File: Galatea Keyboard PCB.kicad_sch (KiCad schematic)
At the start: 0 parts

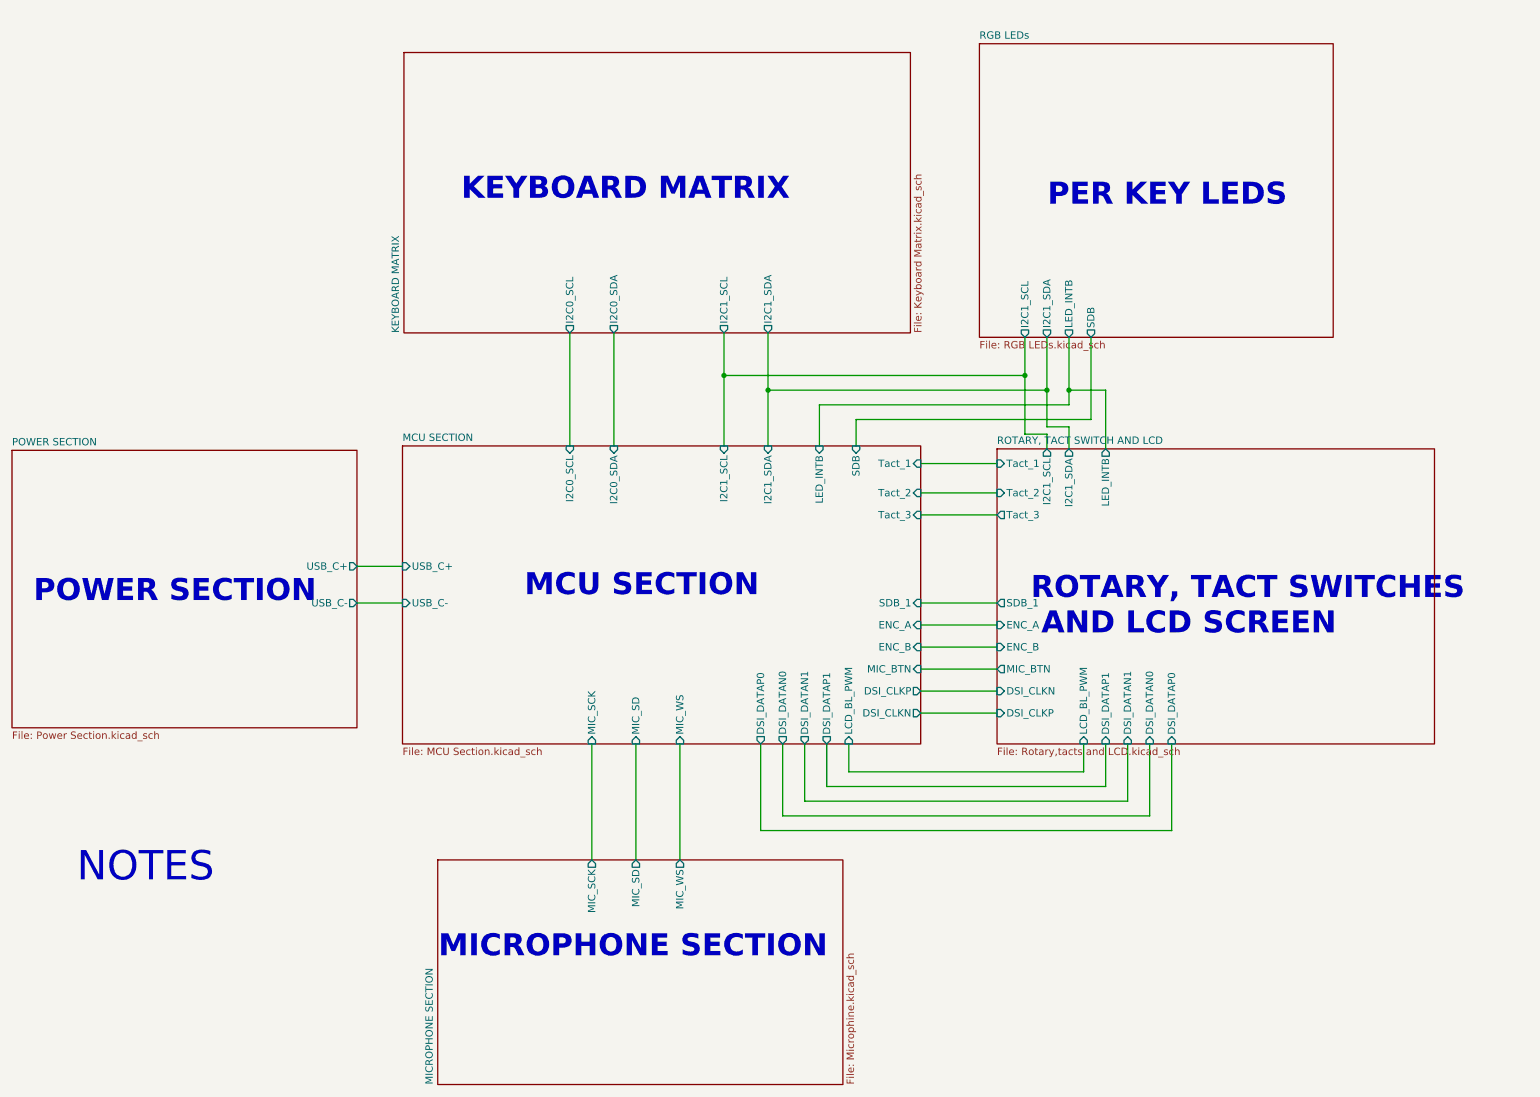
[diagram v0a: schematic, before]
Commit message: Updated the schematic, including power section and the MCU
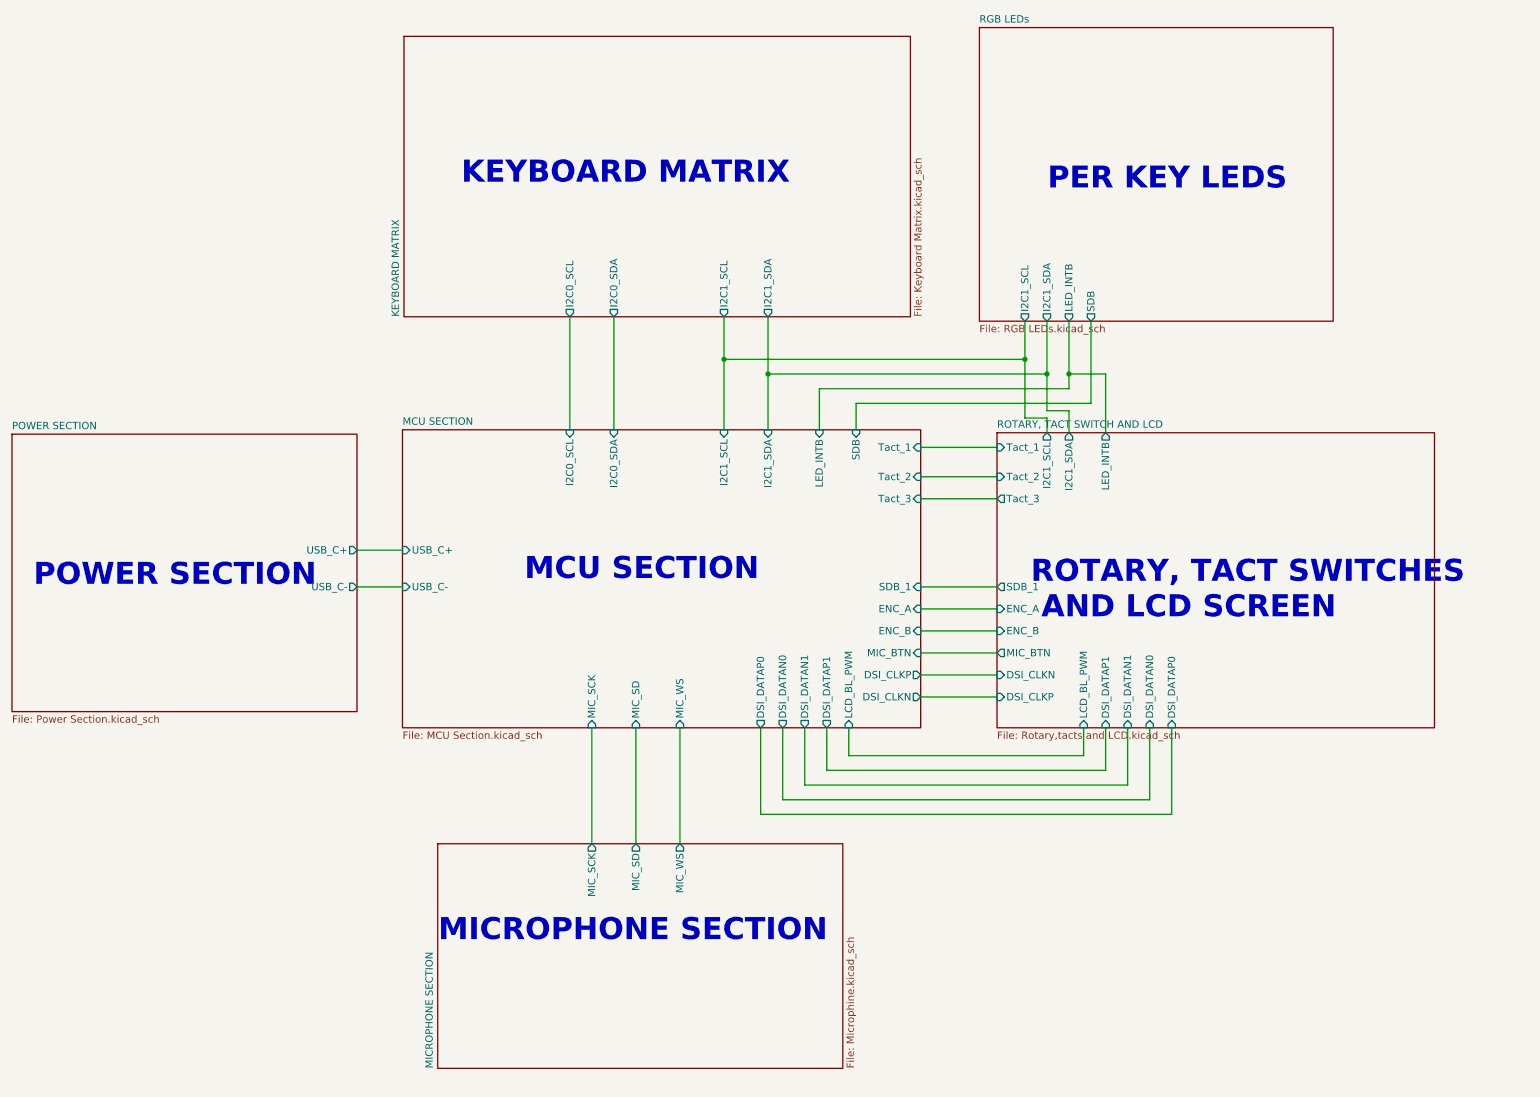
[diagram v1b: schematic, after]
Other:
- note removed: "NOTES"
